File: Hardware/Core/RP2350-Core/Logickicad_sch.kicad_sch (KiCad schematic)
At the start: 45 parts, among them J7 SWD, Q2 2N7002, Q3 2N7002, SW1 TS-1187A-B-A-B, SW2 TS-1187A-B-A-B, U19 W25Q16JVSNIQ, U2 AP2112K-3.3, U3 LM66200DRLR, U4 RP2350A, Y1 Crystal

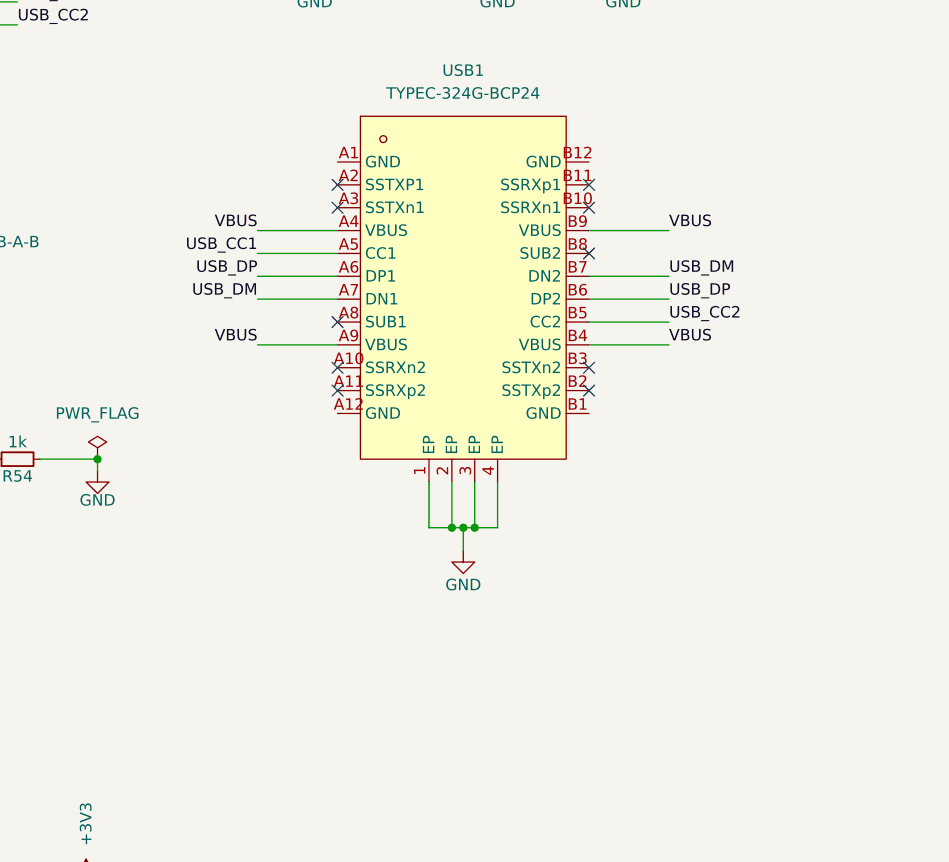
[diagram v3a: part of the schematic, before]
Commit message: Routing core started
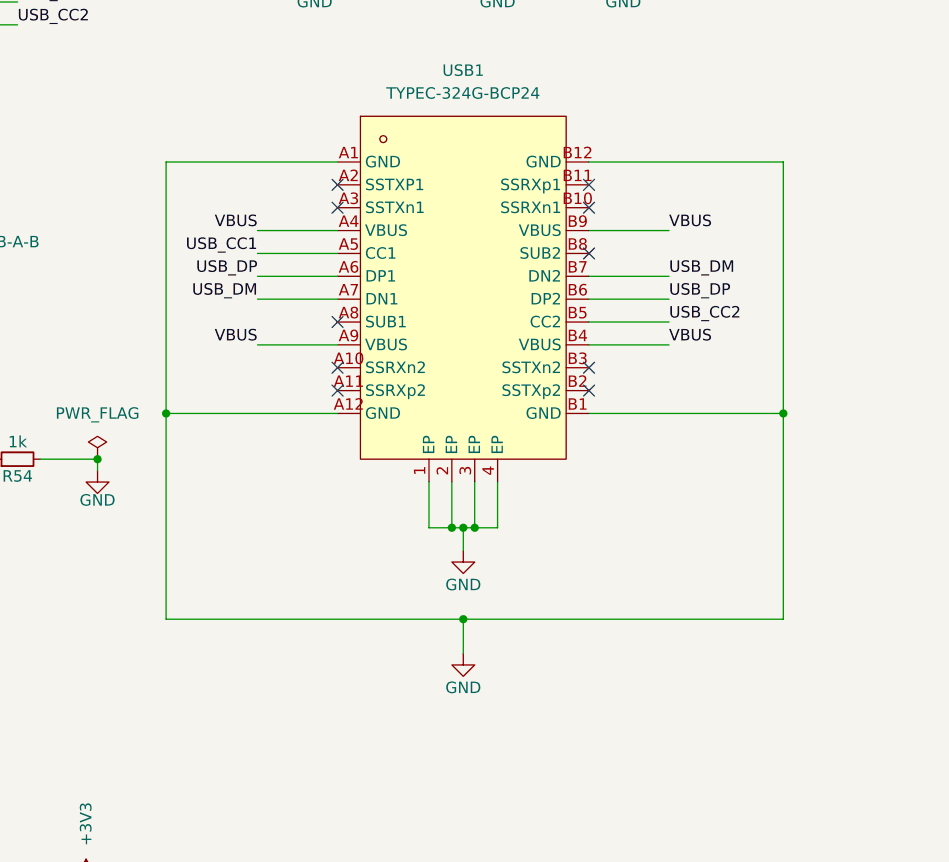
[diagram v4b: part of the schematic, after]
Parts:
- J7: footprint Connector_PinHeader_2.54mm:PinHeader_1x03_P2.54mm_Vertical -> Connector_PinHeader_1.27mm:PinHeader_1x03_P1.27mm_Vertical
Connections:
- net GND: now also USB1.A1 (GND), USB1.A12 (GND), USB1.B1 (GND), USB1.B12 (GND)
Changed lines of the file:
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@@
 	)
 	(junction
+		(at 265.43 168.91)
+		(diameter 0)
+		(color 0 0 0 0)
+	)
+	(junction
 		(at 283.21 86.36)
 		(diameter 0)
@@
 	)
 	(junction
+		(at 300.99 146.05)
+		(diameter 0)
+		(color 0 0 0 0)
+	)
+	(junction
 		(at 165.1 66.04)
 		(diameter 0)
@@
 	)
 	(junction
+		(at 232.41 146.05)
+		(diameter 0)
+		(color 0 0 0 0)
+	)
+	(junction
 		(at 154.94 66.04)
 		(diameter 0)
@@
 	(wire
 		(pts
+			(xy 232.41 146.05) (xy 251.46 146.05)
+		)
+		(stroke
+			(width 0)
+			(type default)
+		)
+	)
+	(wire
+		(pts
 			(xy 96.52 135.89) (xy 111.76 135.89)
 		)
@@
 	(wire
 		(pts
+			(xy 251.46 118.11) (xy 232.41 118.11)
+		)
+		(stroke
+			(width 0)
+			(type default)
+		)
+	)
+	(wire
+		(pts
 			(xy 285.75 59.69) (xy 285.75 69.85)
 		)
@@
 	(wire
 		(pts
+			(xy 232.41 168.91) (xy 265.43 168.91)
+		)
+		(stroke
+			(width 0)
+			(type default)
+		)
+	)
+	(wire
+		(pts
 			(xy 181.61 38.1) (xy 181.61 39.37)
 		)
@@
 	(wire
 		(pts
+			(xy 232.41 118.11) (xy 232.41 146.05)
+		)
+		(stroke
+			(width 0)
+			(type default)
+		)
+	)
+	(wire
+		(pts
 			(xy 351.79 133.35) (xy 367.03 133.35)
 		)
@@
 	(wire
 		(pts
+			(xy 300.99 168.91) (xy 265.43 168.91)
+		)
+		(stroke
+			(width 0)
+			(type default)
+		)
+	)
+	(wire
+		(pts
 			(xy 162.56 113.03) (xy 167.64 113.03)
 		)
@@
 	(wire
 		(pts
+			(xy 232.41 146.05) (xy 232.41 168.91)
+		)
+		(stroke
+			(width 0)
+			(type default)
+		)
+	)
+	(wire
+		(pts
 			(xy 332.74 72.39) (xy 332.74 77.47)
 		)
@@
 	(wire
 		(pts
+			(xy 279.4 118.11) (xy 300.99 118.11)
+		)
+		(stroke
+			(width 0)
+			(type default)
+		)
+	)
+	(wire
+		(pts
 			(xy 194.31 102.87) (xy 203.2 102.87)
 		)
@@
 	(wire
 		(pts
+			(xy 300.99 146.05) (xy 300.99 168.91)
+		)
+		(stroke
+			(width 0)
+			(type default)
+		)
+	)
+	(wire
+		(pts
 			(xy 124.46 62.23) (xy 124.46 80.01)
 		)
@@
 	(wire
 		(pts
+			(xy 265.43 168.91) (xy 265.43 172.72)
+		)
+		(stroke
+			(width 0)
+			(type default)
+		)
+	)
+	(wire
+		(pts
 			(xy 162.56 120.65) (xy 195.58 120.65)
 		)
@@
 	(wire
 		(pts
+			(xy 300.99 118.11) (xy 300.99 146.05)
+		)
+		(stroke
+			(width 0)
+			(type default)
+		)
+	)
+	(wire
+		(pts
 			(xy 96.52 92.71) (xy 111.76 92.71)
 		)
@@
 	(wire
 		(pts
+			(xy 279.4 146.05) (xy 300.99 146.05)
+		)
+		(stroke
+			(width 0)
+			(type default)
+		)
+	)
+	(wire
+		(pts
 			(xy 96.52 123.19) (xy 111.76 123.19)
 		)
@@
 	)
 	(symbol
+		(lib_id "power:GND")
+		(at 265.43 172.72 0)
+		(unit 1)
+		(body_style 1)
+		(exclude_from_sim no)
+		(in_bom yes)
+		(on_board yes)
+		(in_pos_files yes)
+		(dnp no)
+		(property "Reference" "#PWR0104"
+			(at 265.43 179.07 0)
+			(hide yes)
+			(show_name no)
+			(do_not_autoplace no)
+			(effects
+				(font
+					(size 1.27 1.27)
+				)
+			)
+		)
+		(property "Value" "GND"
+			(at 265.43 176.53 0)
+			(show_name no)
+			(do_not_autoplace no)
+			(effects
+				(font
+					(size 1.27 1.27)
+				)
+			)
+		)
+		(property "Footprint" ""
+			(at 265.43 172.72 0)
+			(hide yes)
+			(show_name no)
+			(do_not_autoplace no)
+			(effects
+				(font
+					(size 1.27 1.27)
+				)
+			)
+		)
+		(property "Datasheet" ""
+			(at 265.43 172.72 0)
+			(hide yes)
+			(show_name no)
+			(do_not_autoplace no)
+			(effects
+				(font
+					(size 1.27 1.27)
+				)
+			)
+		)
+		(property "Description" ""
+			(at 265.43 172.72 0)
+			(show_name no)
+			(do_not_autoplace no)
+			(effects
+				(font
+					(size 1.27 1.27)
+				)
+			)
+		)
+		(pin "1"
+		)
+		(instances
+			(project "RP2350-Core"
+				(path "/8bfb0932-e2fe-4425-80ff-903dfd664561/72dc90e8-520e-4b34-baab-d68eea14a92b"
+					(reference "#PWR0104")
+					(unit 1)
+				)
+			)
+		)
+	)
+	(symbol
 		(lib_id "Device:R")
 		(at 207.01 102.87 270)
@@
 			)
 		)
-		(property "Footprint" "Connector_PinHeader_2.54mm:PinHeader_1x03_P2.54mm_Vertical"
+		(property "Footprint" "Connector_PinHeader_1.27mm:PinHeader_1x03_P1.27mm_Vertical"
 			(at 173.99 161.29 0)
 			(hide yes)

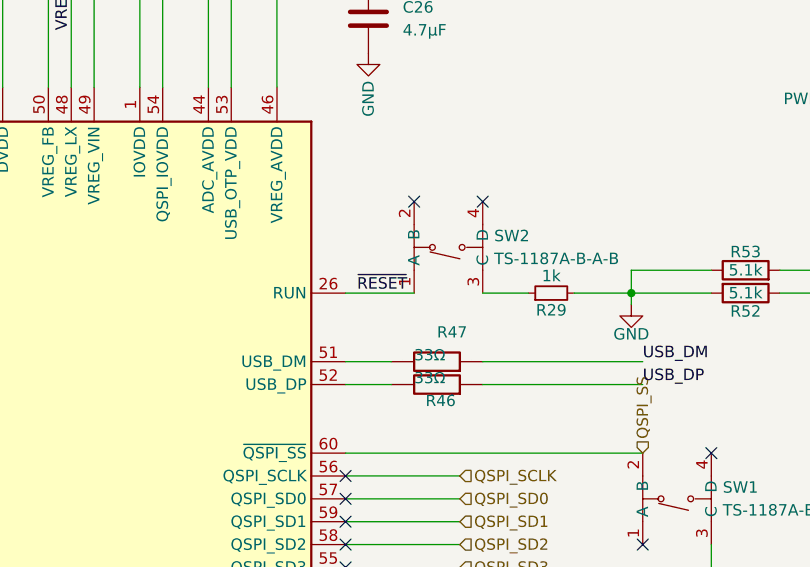
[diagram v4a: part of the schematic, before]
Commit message: RP235X Layout complete
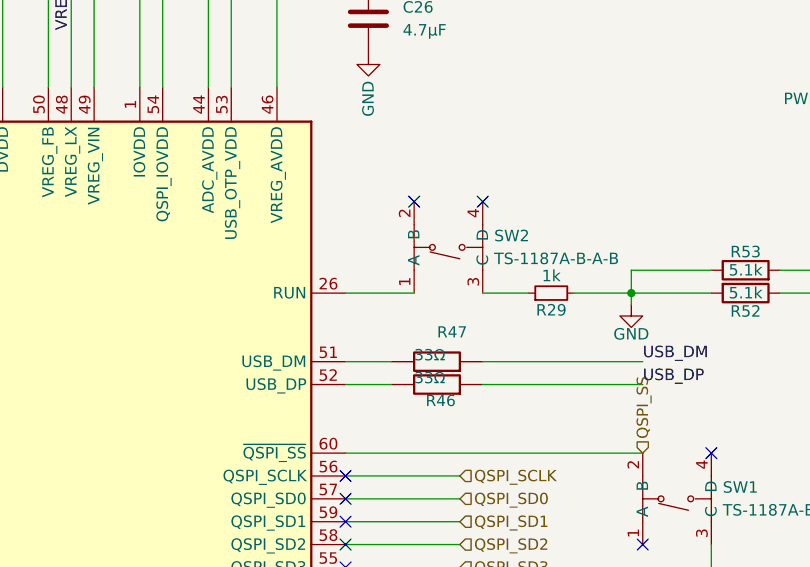
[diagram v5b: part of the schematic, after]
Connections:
- net ~{RESET}: no longer SW2.1 (A), U4.26 (RUN)
- new net: SW2.1 (A), U4.26 (RUN)
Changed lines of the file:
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@@
-		)
-	)
-	(label "~{RESET}"
-		(at 163.83 102.87 0)
-		(effects
-			(font
-				(size 1.27 1.27)
-			)
-			(justify left bottom)
 		)
 	)
